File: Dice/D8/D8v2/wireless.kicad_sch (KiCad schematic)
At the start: 29 parts, among them J3 Conn_01x02, P5 COILA, P6 COILB, U3 PJ75AL50SA, U5 MCP73832T-2ACI/OT

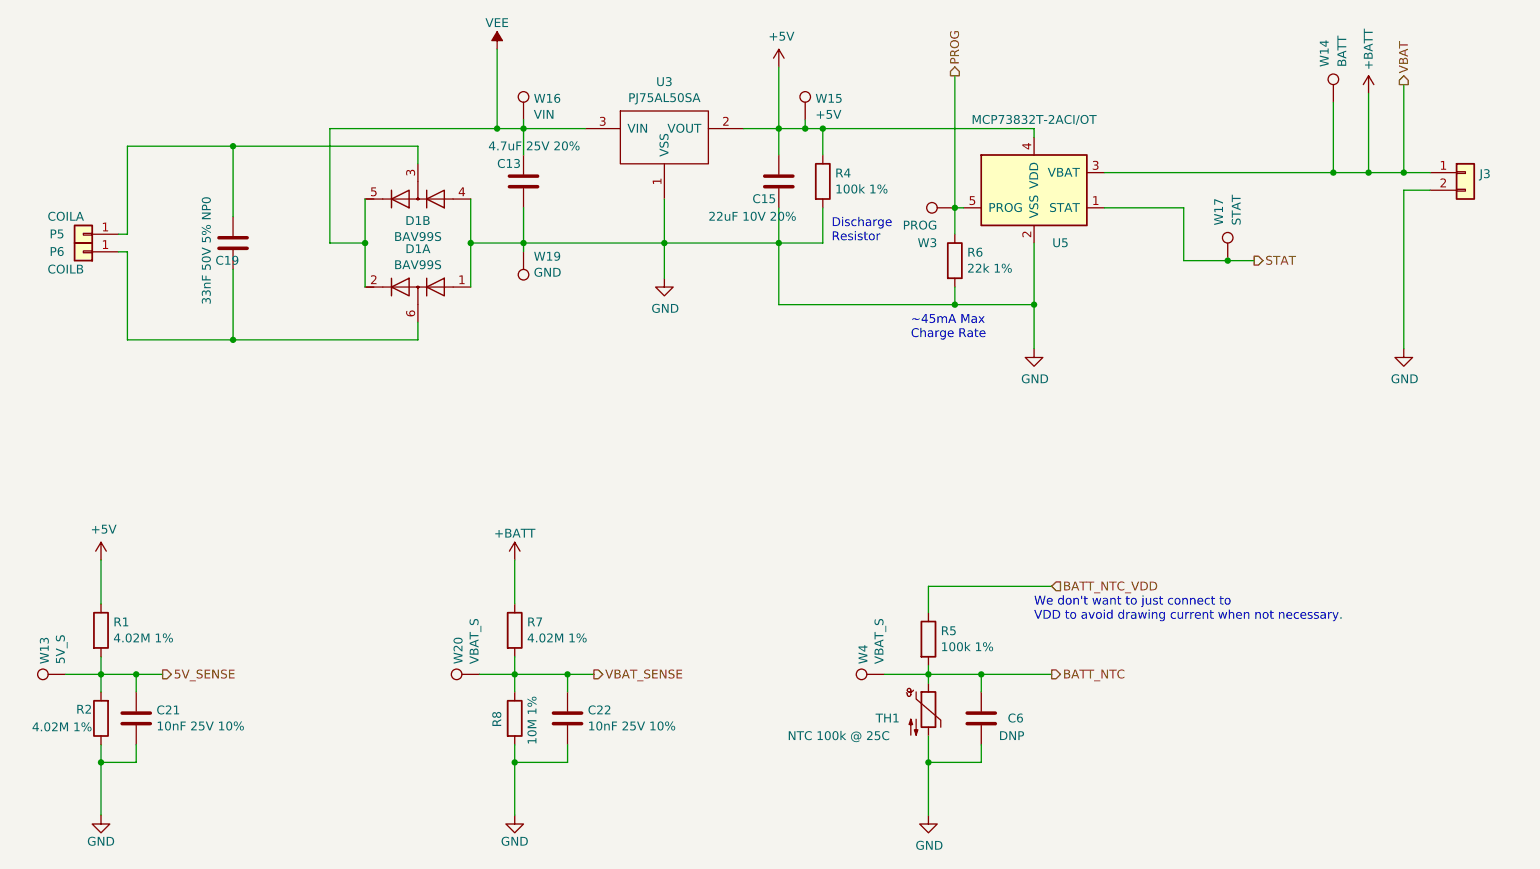
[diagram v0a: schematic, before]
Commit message: Updated all remaining boards to match D20V15 (D6, PD6, D8, D10 and D12)
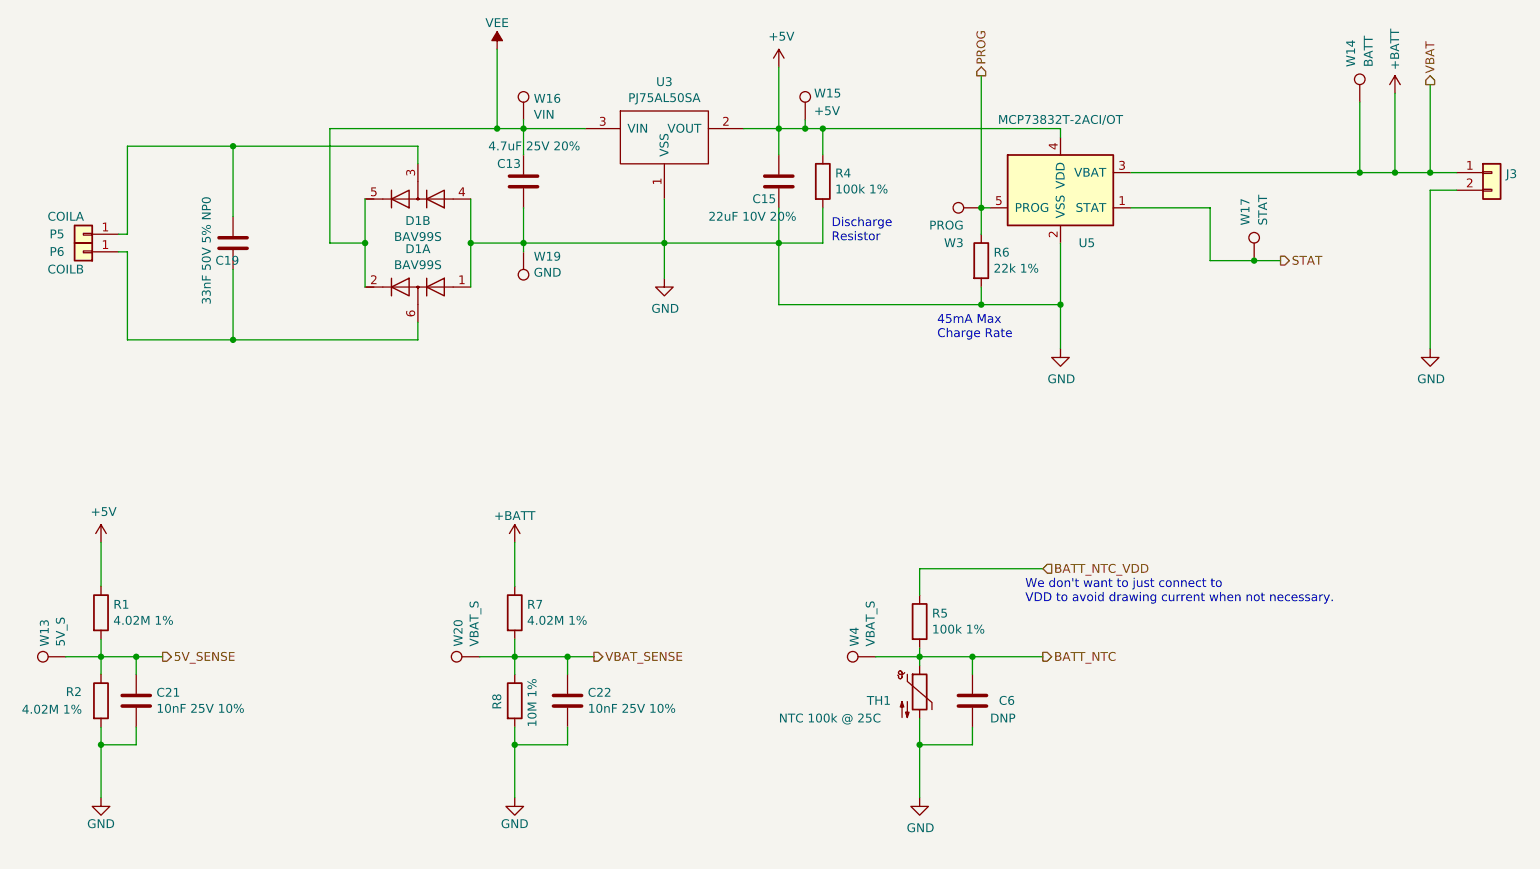
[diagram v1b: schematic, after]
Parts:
- R2: Pixels Part Number SMD-R004 -> SMD-R003
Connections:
- net 5V_SENSE: now also R2.1; no longer R2.2
- net GND: now also R2.2; no longer R2.1
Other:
- note added: "45mA Max Charge Rate"
- note removed: "~45mA Max Charge Rate"
- moved on the sheet: C21, C22, J3, R1, R6, R7, R8, U5, W13, W14, W17, W20
